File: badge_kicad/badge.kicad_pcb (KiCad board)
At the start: 2 copper layers, 76.9 x 42.2 mm, 19 parts, among them P2 Pin, P3 Pin, P4 Pin, P5 Pin, P6 Pin, SW1 ON

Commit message: rev2 mockup
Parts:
- removed BT2: BATT_2, badge_fp:cr2032_02
- removed D3: Blu, badge_fp:LED-5MM
- removed D4: Wht, badge_fp:LED-5MM
- removed the G*** at (36.8, 43.2)
- removed the G*** at (50.8, 52.1)
- removed the G*** at (68.6, 43.8)
- removed R3, R4: 10E, badge_fp:r_0805
- added G***: LOGO, badge_fp:create3, F.Cu at (79.4, 39.4)
- added G***: LOGO, badge_fp:make3, F.Cu at (69.2, 31.8)
- added G***: LOGO, badge_fp:break3, F.Cu at (73.7, 35.6)
- added G***: LOGO, badge_fp:Logo_silk_OSHW_6x6mm, F.Cu at (50.2, 64.1)
- added G***: LOGO, badge_fp:MA_LOGO10, F.Cu at (61.0, 45.1)
- added P4: Pin, badge_fp:MTG_0mm8, F.Cu at (96.5, 49.5)
- added P5: Pin, badge_fp:MTG_0mm8, F.Cu at (42.5, 35.6)
- moved D2 52.2 mm to (86.4, 47.0), turned to 90 degrees
- moved R2 36.1 mm to (86.4, 52.1)
- moved P2 30.3 mm to (61.0, 35.6)
- moved R1 22.4 mm to (31.8, 41.9), turned to 180 degrees
- moved P6 21.6 mm to (79.4, 35.6)
- moved P5 6.48 mm to (53.3, 35.6)
- moved P3 5.46 mm to (68.6, 35.6)
- moved D1 4.07 mm to (31.8, 47.0)
- moved SW1 3.86 mm to (61.0, 57.8)
- moved BT1 3.48 mm to (47.6, 47.0), turned to 180 degrees
- moved P4 0.63 mm to (25.4, 49.5)

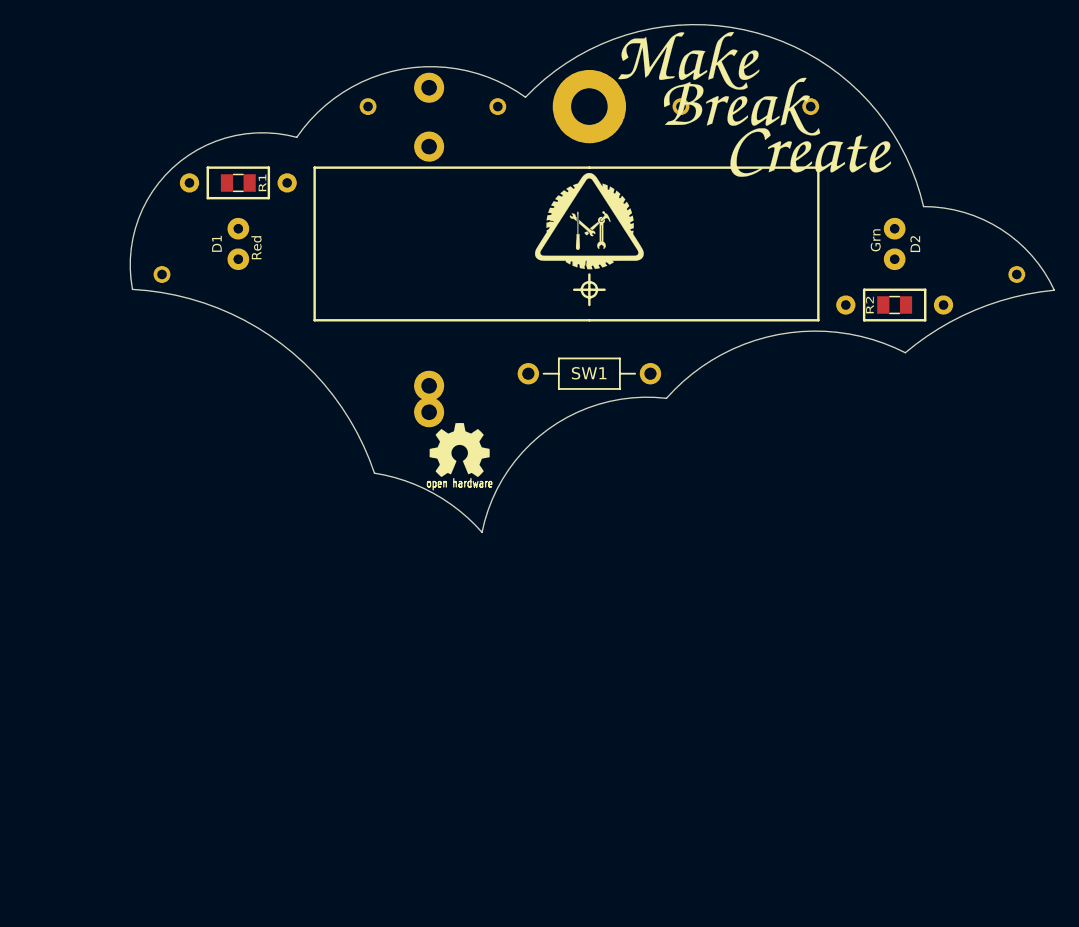
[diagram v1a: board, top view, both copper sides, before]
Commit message: PCB sharp edges rounded
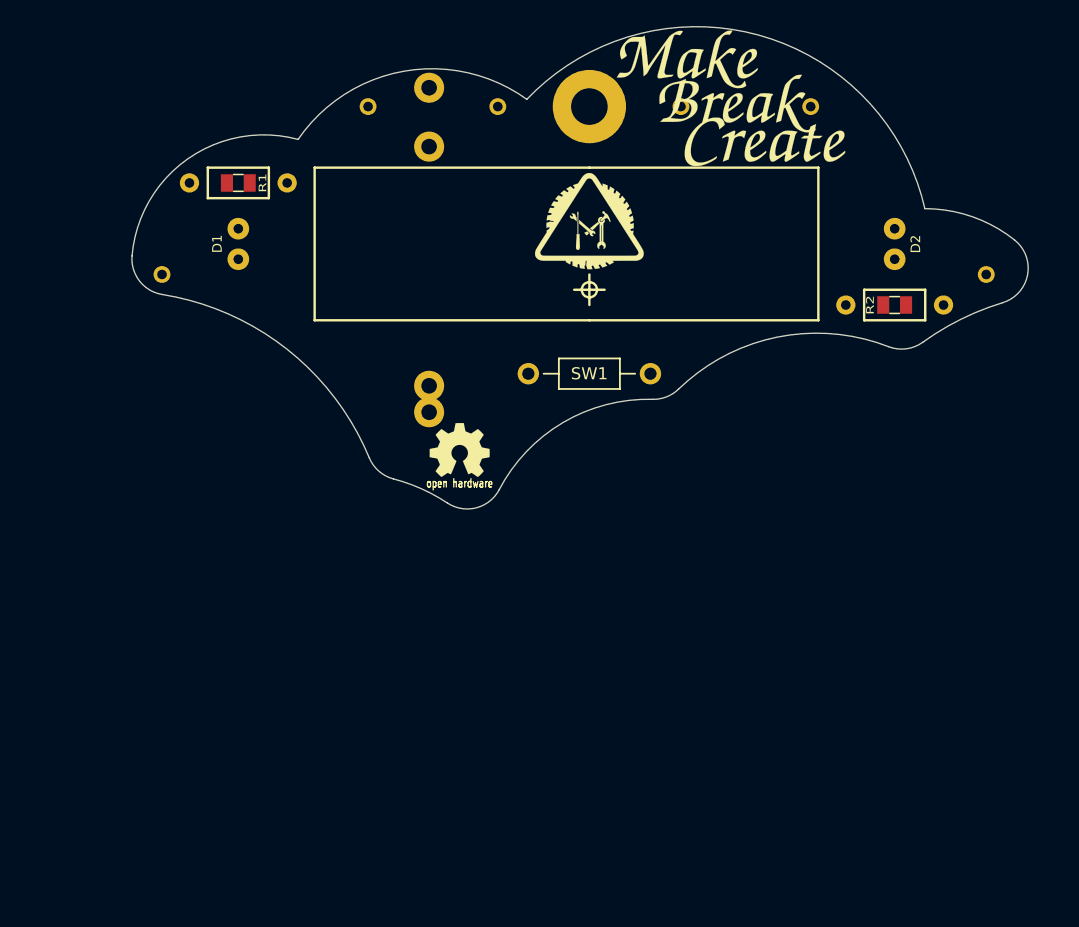
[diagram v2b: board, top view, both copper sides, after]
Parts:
- moved G*** 3.91 mm to (75.6, 38.5)
- moved P4 2.54 mm to (94.0, 49.5)
- moved G*** 0.46 mm to (73.3, 35.3)
- moved G*** 0.18 mm to (69.1, 31.6)
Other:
- board size 76.9 x 42.2 mm -> 74.6 x 40.1 mm
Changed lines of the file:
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@@
     (links 13)
     (no_connects 13)
-    (area 21.705999 20.16 101.806001 80.929001)
+    (area 21.705999 20.16 101.917742 81.101671)
     (thickness 1.6)
-    (drawings 19)
+    (drawings 34)
     (tracks 0)
     (zones 0)
@@
     (zone_45_only no)
     (trace_min 0.2)
-    (segment_width 0.2)
+    (segment_width 0.15)
     (edge_width 0.15)
     (via_size 0.6)
@@
   )
   (module badge_fp:MTG_0mm8 (layer F.Cu)
-    (at 96.52 49.53)
+    (at 93.98 49.53)
     (fp_text reference P4 (at 0 1.27) (layer F.SilkS) hide
       (effects (font (size 1 1) (thickness 0.15)))
@@
       (effects (font (size 0.8 0.8) (thickness 0.15)))
     )
-    (fp_text value Red (at 0.316987 -1.549038 270) (layer F.SilkS)
+    (fp_text value Red (at 0.316987 -1.549038 270) (layer F.SilkS) hide
       (effects (font (size 0.8 0.8) (thickness 0.15)))
     )
@@
       (effects (font (size 0.8 0.8) (thickness 0.15)))
     )
-    (fp_text value Grn (at 0.316987 -1.549038 90) (layer F.SilkS)
+    (fp_text value Grn (at 0.316987 -1.549038 90) (layer F.SilkS) hide
       (effects (font (size 0.8 0.8) (thickness 0.15)))
     )
@@
   )
   (module badge_fp:create3 (layer F.Cu)
-    (at 79.375 39.37)
+    (at 75.565 38.481)
     (fp_text reference G*** (at 0 0) (layer F.SilkS) hide
       (effects (font (thickness 0.3)))
@@
   )
   (module badge_fp:make3 (layer F.Cu)
-    (at 69.215 31.75)
+    (at 69.088 31.623)
     (fp_text reference G*** (at 0 0) (layer F.SilkS) hide
       (effects (font (thickness 0.3)))
@@
   )
   (module badge_fp:break3 (layer F.Cu)
-    (at 73.66 35.56)
+    (at 73.279 35.306)
     (fp_text reference G*** (at 0 0) (layer F.SilkS) hide
       (effects (font (thickness 0.3)))
@@
       (xy -1.443125 -0.627927) (xy -1.402959 -0.632909) (xy -1.359647 -0.632585)) (layer F.SilkS) (width 0.01))
   )
+  (gr_arc (start 40.867741 81.05167) (end 49.144624 68.541945) (angle -18.8411851) (layer Edge.Cuts) (width 0.1))
+  (gr_arc (start 45.419844 63.636781) (end 42.649008 64.786768) (angle -52.81109566) (layer Edge.Cuts) (width 0.1))
+  (gr_arc (start 21.867741 73.41167) (end 42.649008 64.786768) (angle -58.36929602) (layer Edge.Cuts) (width 0.1))
+  (gr_arc (start 25.896669 48.231961) (end 22.907516 47.97707) (angle -85.78326535) (layer Edge.Cuts) (width 0.1))
+  (gr_arc (start 33.867741 48.91167) (end 36.725461 38.289361) (angle -100.1838296) (layer Edge.Cuts) (width 0.1))
+  (gr_arc (start 47.867741 45.91167) (end 55.754837 34.955224) (angle -91.37297389) (layer Edge.Cuts) (width 0.1))
+  (gr_arc (start 101.867741 73.41167) (end 95.34066 51.879201) (angle -18.97193507) (layer Edge.Cuts) (width 0.1))
+  (gr_arc (start 86.938524 52.738777) (end 85.850706 55.534605) (angle -57.09601192) (layer Edge.Cuts) (width 0.1))
+  (gr_arc (start 79.867741 70.91167) (end 85.850706 55.534605) (angle -65.39679548) (layer Edge.Cuts) (width 0.1))
+  (gr_arc (start 69.867741 48.41167) (end 88.874067 44.051672) (angle -123.4440611) (layer Edge.Cuts) (width 0.1))
+  (gr_arc (start 88.867741 56.05167) (end 96.337931 46.660383) (angle -38.46988455) (layer Edge.Cuts) (width 0.1))
+  (gr_arc (start 94.470383 49.008205) (end 95.34066 51.879201) (angle -124.6364262) (layer Edge.Cuts) (width 0.1))
+  (gr_arc (start 66.2885 56.916878) (end 66.214249 59.915959) (angle -45.55482387) (layer Edge.Cuts) (width 0.1))
+  (gr_arc (start 65.867741 73.91167) (end 66.214249 59.915959) (angle -63.83483999) (layer Edge.Cuts) (width 0.1))
+  (gr_arc (start 50.8 66.04) (end 49.144624 68.541945) (angle -95.90664011) (layer Edge.Cuts) (width 0.1))
   (gr_line (start 80.01 40.64) (end 60.96 40.64) (layer F.SilkS) (width 0.2))
   (gr_line (start 80.01 53.34) (end 80.01 40.64) (layer F.SilkS) (width 0.2))
@@
   (gr_circle (center 60.96 50.8) (end 60.325 50.8) (layer F.SilkS) (width 0.2))
   (gr_line (start 60.96 49.53) (end 60.96 52.07) (layer F.SilkS) (width 0.2))
-  (dimension 76.708 (width 0.3) (layer Dwgs.User)
-    (gr_text "3.0200 in" (at 61.214 21.51) (layer Dwgs.User)
+  (dimension 74.676 (width 0.3) (layer Dwgs.User)
+    (gr_text "2.9400 in" (at 60.198 21.51) (layer Dwgs.User)
       (effects (font (size 1.5 1.5) (thickness 0.3)))
     )
-    (feature1 (pts (xy 99.568 50.8) (xy 99.568 20.16)))
+    (feature1 (pts (xy 97.536 50.8) (xy 97.536 20.16)))
     (feature2 (pts (xy 22.86 50.8) (xy 22.86 20.16)))
-    (crossbar (pts (xy 22.86 22.86) (xy 99.568 22.86)))
-    (arrow1a (pts (xy 99.568 22.86) (xy 98.441496 23.446421)))
-    (arrow1b (pts (xy 99.568 22.86) (xy 98.441496 22.273579)))
+    (crossbar (pts (xy 22.86 22.86) (xy 97.536 22.86)))
+    (arrow1a (pts (xy 97.536 22.86) (xy 96.409496 23.446421)))
+    (arrow1b (pts (xy 97.536 22.86) (xy 96.409496 22.273579)))
     (arrow2a (pts (xy 22.86 22.86) (xy 23.986504 23.446421)))
     (arrow2b (pts (xy 22.86 22.86) (xy 23.986504 22.273579)))
   )
-  (gr_arc (start 88.756 55.879) (end 99.645902 50.838163) (angle -65.1308075) (layer Edge.Cuts) (width 0.1))
-  (gr_arc (start 101.756 73.239) (end 99.645902 50.838163) (angle -34.76178927) (layer Edge.Cuts) (width 0.1))
-  (gr_arc (start 47.756 45.739) (end 55.643096 34.782554) (angle -91.37297389) (layer Edge.Cuts) (width 0.1))
-  (gr_arc (start 69.756 48.239) (end 88.762326 43.879002) (angle -123.4440611) (layer Edge.Cuts) (width 0.1))
-  (gr_arc (start 21.756 73.239) (end 43.08002 66.060129) (angle -68.36415079) (layer Edge.Cuts) (width 0.1))
-  (gr_arc (start 33.756 48.739) (end 36.61372 38.116691) (angle -115.7000736) (layer Edge.Cuts) (width 0.1))
-  (gr_arc (start 65.756 73.739) (end 67.374325 59.832849) (angle -85.29031279) (layer Edge.Cuts) (width 0.1))
-  (gr_arc (start 40.756 80.879) (end 52.029679 70.984347) (angle -39.81430139) (layer Edge.Cuts) (width 0.1))
-  (gr_arc (start 79.756 70.739) (end 87.250301 56.039154) (angle -75.63890877) (layer Edge.Cuts) (width 0.1))
+  (gr_arc (start 88.756 55.879) (end 99.645902 50.838163) (angle -65.1) (layer Eco1.User) (width 0.1))
+  (gr_arc (start 101.756 73.239) (end 99.645902 50.838163) (angle -34.7) (layer Eco1.User) (width 0.1))
+  (gr_arc (start 47.756 45.739) (end 55.643096 34.782554) (angle -91.3) (layer Eco1.User) (width 0.1))
+  (gr_arc (start 69.756 48.239) (end 88.762326 43.879002) (angle -123.4) (layer Eco1.User) (width 0.1))
+  (gr_arc (start 21.756 73.239) (end 43.08002 66.060129) (angle -68.3) (layer Eco1.User) (width 0.1))
+  (gr_arc (start 33.756 48.739) (end 36.61372 38.116691) (angle -115.7) (layer Eco1.User) (width 0.1))
+  (gr_arc (start 65.756 73.739) (end 67.374325 59.832849) (angle -85.2) (layer Eco1.User) (width 0.1))
+  (gr_arc (start 40.756 80.879) (end 52.029679 70.984347) (angle -39.8) (layer Eco1.User) (width 0.1))
+  (gr_arc (start 79.756 70.739) (end 87.250301 56.039154) (angle -75.6) (layer Eco1.User) (width 0.1))
 )

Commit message: outline modified
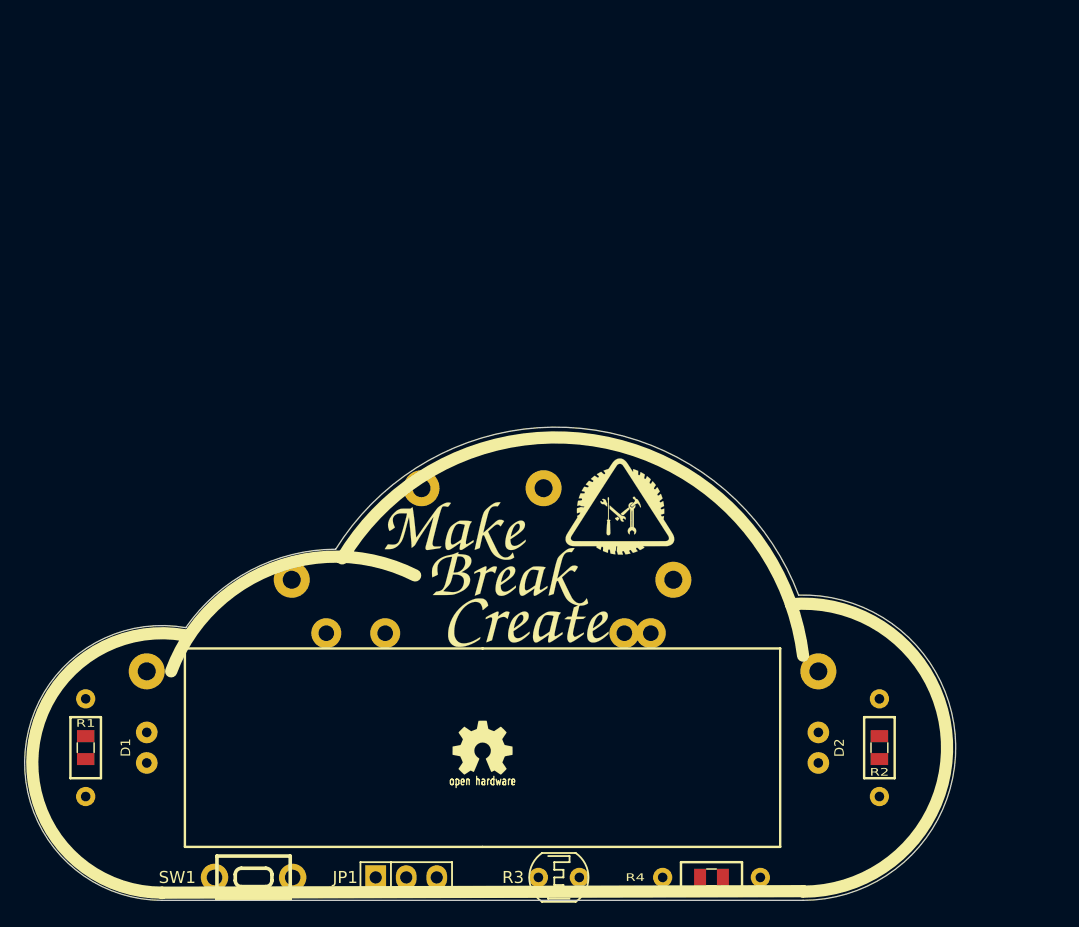
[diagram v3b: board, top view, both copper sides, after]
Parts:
- removed the G*** at (61.0, 45.1)
- removed the P2 at (61.0, 35.6)
- added JP1: JMP, badge_fp:Pin_Header_Straight_1x03, F.Cu at (43.2, 99.7)
- added L1: Logo_MA, badge_fp:MA_LOGO10, F.Cu at (63.5, 68.8)
- added R3: LDR, badge_fp:Resistor_LDR_5.0x3.4, F.Cu at (58.4, 99.7)
- added R4: 10E, badge_fp:r_0805, F.Cu at (71.1, 99.7)
- P1, P3: renamed from P5; footprint badge_fp:MTG_0mm8 -> badge_fp:MTG_1mm5
- P2: renamed from P3; footprint badge_fp:MTG_0mm8 -> badge_fp:MTG_1mm5
- P4: renamed from P6; footprint badge_fp:MTG_0mm8 -> badge_fp:MTG_1mm5
- P5, P6: renamed from P4; footprint badge_fp:MTG_0mm8 -> badge_fp:MTG_1mm5
- SW1: footprint badge_fp:Resistor_Horizontal_RM10mm -> badge_fp:switch_MJTP1250
- moved SW1 50.4 mm to (33.0, 99.7), turned to 180 degrees
- moved R1 48.7 mm to (19.1, 88.9), turned to 270 degrees
- moved G*** 44.6 mm to (55.9, 78.5)
- moved G*** 43.7 mm to (49.8, 70.9)
- moved G*** 43.7 mm to (54.4, 74.7)
- moved D1 42.6 mm to (24.1, 88.9)
- moved D2 42.4 mm to (80.0, 88.9)
- moved P4 41.0 mm to (67.9, 74.9)
- moved P3 39.9 mm to (36.2, 74.9)
- moved R2 36.9 mm to (85.1, 88.9), turned to 90 degrees
- moved P6 35.9 mm to (80.0, 82.5)
- moved P2 33.7 mm to (57.1, 67.3)
- moved P5 33.0 mm to (24.1, 82.5)
- moved BT1 32.7 mm to (52.1, 79.4), turned to 270 degrees
- moved P1 32.4 mm to (47.0, 67.3)
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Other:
- board size 74.6 x 40.1 mm -> 77.5 x 39.4 mm

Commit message: track layout
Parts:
- added P2: Pin, badge_fp:MTG_0mm8, F.Cu at (33.0, 78.7)
- added P2: Pin, badge_fp:MTG_0mm8, F.Cu at (35.6, 78.7)
- added P2: Pin, badge_fp:MTG_0mm8, F.Cu at (33.0, 76.2)
- added P2: Pin, badge_fp:MTG_0mm8, F.Cu at (73.7, 78.7)
- added P2: Pin, badge_fp:MTG_0mm8, F.Cu at (71.1, 78.7)
- added P2: Pin, badge_fp:MTG_0mm8, F.Cu at (76.2, 78.7)
- added P2: Pin, badge_fp:MTG_0mm8, F.Cu at (73.7, 76.2)
- added P2: Pin, badge_fp:MTG_0mm8, F.Cu at (71.1, 76.2)
- added P2: Pin, badge_fp:MTG_0mm8, F.Cu at (71.1, 73.7)
- added P2: Pin, badge_fp:MTG_0mm8, F.Cu at (73.7, 73.7)
- added P2: Pin, badge_fp:MTG_0mm8, F.Cu at (25.4, 99.1)
- added P2: Pin, badge_fp:MTG_0mm8, F.Cu at (76.2, 76.2)
- added P2: Pin, badge_fp:MTG_0mm8, F.Cu at (71.1, 71.1)
- added P2: Pin, badge_fp:MTG_0mm8, F.Cu at (25.4, 96.5)
- added P2: Pin, badge_fp:MTG_0mm8, F.Cu at (25.4, 94.0)
- added P2: Pin, badge_fp:MTG_0mm8, F.Cu at (22.9, 94.0)
- added P2: Pin, badge_fp:MTG_0mm8, F.Cu at (22.9, 96.5)
- added P2: Pin, badge_fp:MTG_0mm8, F.Cu at (22.9, 99.1)
- added P2: Pin, badge_fp:MTG_0mm8, F.Cu at (20.3, 96.5)
- added P2: Pin, badge_fp:MTG_0mm8, F.Cu at (30.5, 78.7)
- added Q1: 2N3904, badge_fp:TO-92_Inline_Wide, F.Cu at (78.7, 96.5)
- L2: renamed from G***; value LOGO -> Make
- L3: renamed from G***; value LOGO -> Break
- L4: renamed from G***; value LOGO -> Create
- L5: renamed from G***; value LOGO -> OSHW
- R1, R2: value 10E -> 100E
- R4: value 10E -> 47k
- moved R4 12.7 mm to (58.4, 99.4)
- moved R3 8.64 mm to (67.1, 99.4)
- moved JP1 0.25 mm to (43.2, 99.4)
- moved SW1 0.25 mm to (33.0, 99.4)
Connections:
- R1 pad 1: /GND -> Net-(Q1-Pad1)
- R2 pad 1: /GND -> Net-(Q1-Pad1)
- R3 pad 1: /3V -> Net-(Q1-Pad2)
- R3 pad 2: /[+] -> /GND
- R4 pad 1: /[+] -> /3V
- R4 pad 2: /3V -> Net-(Q1-Pad2)
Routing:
- net /3V: track 0.00 -> 137.3 mm
- net /[+]: track 0.00 -> 103.1 mm
- net Net-(Q1-Pad1): track 0.00 -> 84.5 mm
- net /GND: track 0.00 -> 59.6 mm
- net Net-(Q1-Pad2): track 0.00 -> 25.6 mm
- net /LED_grn: track 0.00 -> 8.33 mm
- net /LED_red: track 0.00 -> 8.33 mm
- added copper zone on F.Cu, net /3V
- added copper zone on B.Cu, net /GND
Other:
- net class 10 mil added: clearance 0.2032, trace_width 0.254, via_dia 0.6, via_drill 0.4
- net class 15 mil added: clearance 0.2032, trace_width 0.381, via_dia 0.6, via_drill 0.4
- net class 20 mil added: clearance 0.2032, trace_width 0.508, via_dia 0.6, via_drill 0.4
- board text added: "S.T.E.A.M. Badge"
- board text added: "https://git.io/vdyeU"
- board text added: "www.makersasylum.com"

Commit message: gerbers generated, ready
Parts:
- added L6: KiCad, badge_fp:KiCad-Logo2_6mm_SilkScreen, B.Cu at (52.7, 79.4)
- L1: value Logo_MA -> ma_logo
- Q1: value 2N3904 -> 2N2222
- moved R3 4.06 mm to (71.1, 99.4)
- turned R1 to 90 degrees
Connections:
- net Net-(Q1-Pad1) renamed /Coll
- net Net-(Q1-Pad2) renamed /Base
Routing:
- net /GND: track 59.6 -> 82.6 mm
- net /3V: track 137.3 -> 124.1 mm
- net /Coll: track 84.5 -> 76.1 mm
- net /[+]: track 103.1 -> 105.0 mm
- net /LED_red: track 8.33 -> 9.11 mm
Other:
- board text added: "[+]"
- board text added: "[-]"

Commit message: final gerbers, ready for production
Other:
- board text added: "S.T.E.A.M. School"
- board text removed: "S.T.E.A.M. Badge"
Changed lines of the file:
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@@
     (visible_elements FFFFEF7F)
     (pcbplotparams
-      (layerselection 0x00130_80000001)
-      (usegerberextensions false)
-      (excludeedgelayer false)
+      (layerselection 0x010f0_80000001)
+      (usegerberextensions true)
+      (excludeedgelayer true)
       (linewidth 0.101600)
-      (plotframeref true)
+      (plotframeref false)
       (viasonmask false)
       (mode 1)
@@
       (plotvalue true)
       (plotinvisibletext false)
-      (padsonsilk true)
-      (subtractmaskfromsilk false)
-      (outputformat 4)
+      (padsonsilk false)
+      (subtractmaskfromsilk true)
+      (outputformat 1)
       (mirror false)
-      (drillshape 2)
+      (drillshape 0)
       (scaleselection 1)
-      (outputdirectory pdf/))
+      (outputdirectory gerber/))
   )
   (net 0 "")
@@
     (effects (font (size 1.27 1.27) (thickness 0.254)) (justify mirror))
   )
-  (gr_text "S.T.E.A.M. Badge" (at 66.04 94.615) (layer B.SilkS)
+  (gr_text "S.T.E.A.M. School" (at 66.04 94.615) (layer B.SilkS)
     (effects (font (thickness 0.3048)) (justify mirror))
   )
